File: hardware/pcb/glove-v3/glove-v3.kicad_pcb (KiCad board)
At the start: 2 copper layers, 18 parts, among them U1 XIAO-ESP32C3, U2 CD74HC4067M96

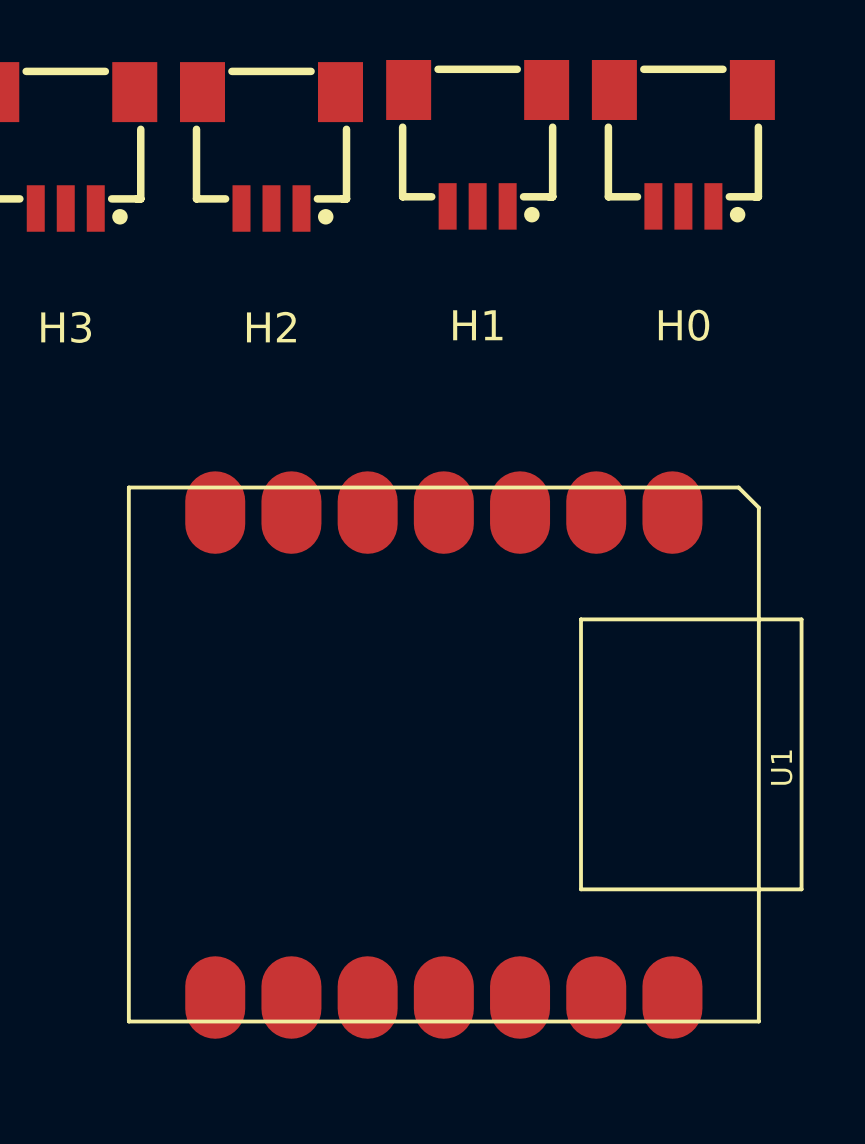
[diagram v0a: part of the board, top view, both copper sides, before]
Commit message: added decoupling capacitor and updated footprints
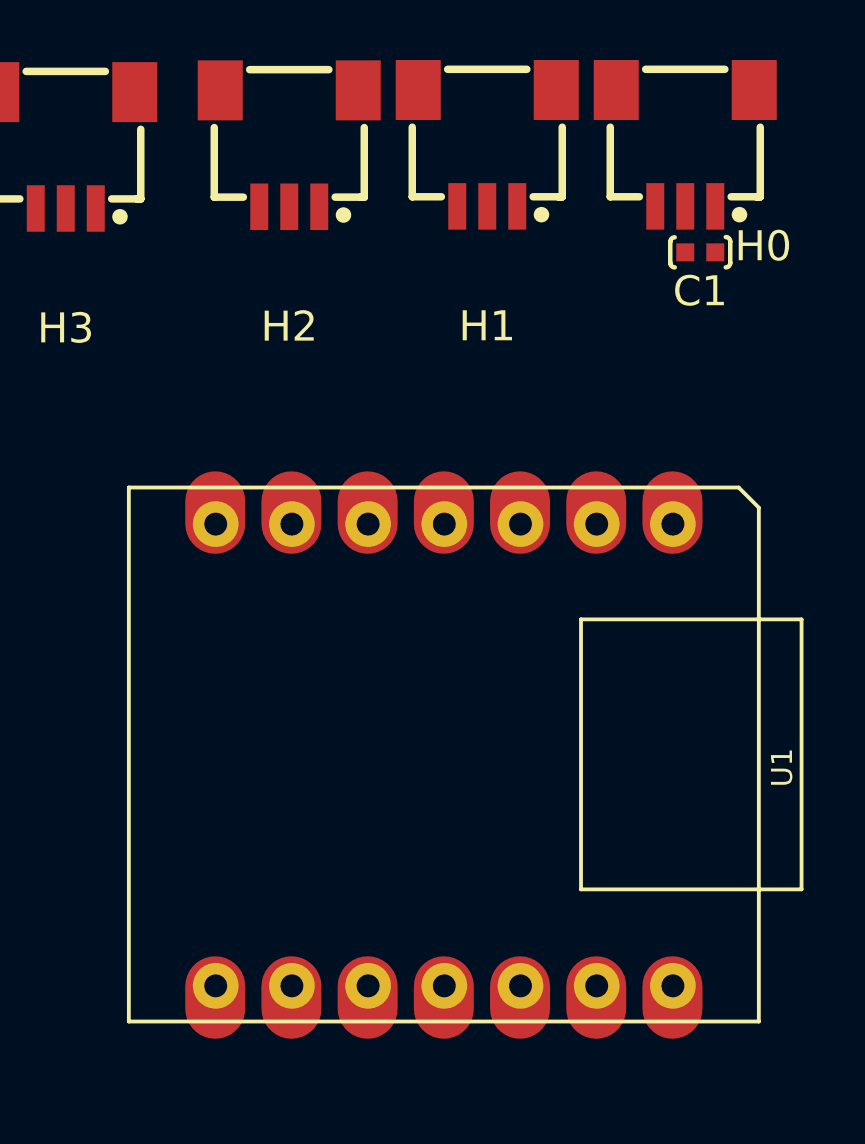
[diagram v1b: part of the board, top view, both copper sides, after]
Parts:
- added C1: C-0402-0.01uF, 0_easyeda2kicad:C0402, F.Cu at (177.6, 37.6)
- moved H2 0.59 mm to (163.9, 34.1)
- moved H1 0.32 mm to (170.5, 34.1)
- moved H0 0.06 mm to (177.1, 34.1)

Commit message: schematic done and board layout done
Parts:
- added C0: C-0402-0.01uF, 0_easyeda2kicad:C0402, F.Cu at (108.6, 56.2)
- added C10: C-0402-0.01uF, 0_easyeda2kicad:C0402, F.Cu at (143.7, 31.9)
- added C11: C-0402-0.01uF, 0_easyeda2kicad:C0402, F.Cu at (150.2, 31.9)
- added C12: C-0402-0.01uF, 0_easyeda2kicad:C0402, F.Cu at (156.7, 31.9)
- added C13: C-0402-0.01uF, 0_easyeda2kicad:C0402, F.Cu at (163.2, 31.9)
- added C14: C-0402-0.01uF, 0_easyeda2kicad:C0402, F.Cu at (169.7, 31.9)
- added C15: C-0402-0.01uF, 0_easyeda2kicad:C0402, F.Cu at (176.2, 31.9)
- added C2: C-0402-0.01uF, 0_easyeda2kicad:C0402, F.Cu at (108.6, 43.2)
- added C3: C-0402-0.01uF, 0_easyeda2kicad:C0402, F.Cu at (108.6, 36.7)
- added C4: C-0402-0.01uF, 0_easyeda2kicad:C0402, F.Cu at (104.7, 31.9)
- added C5: C-0402-0.01uF, 0_easyeda2kicad:C0402, F.Cu at (111.2, 31.9)
- added C6: C-0402-0.01uF, 0_easyeda2kicad:C0402, F.Cu at (117.7, 31.9)
- added C7: C-0402-0.01uF, 0_easyeda2kicad:C0402, F.Cu at (124.2, 31.9)
- added C8: C-0402-0.01uF, 0_easyeda2kicad:C0402, F.Cu at (130.7, 31.9)
- added C9: C-0402-0.01uF, 0_easyeda2kicad:C0402, F.Cu at (137.2, 31.9)
- added REF**: MountingHole_2.2mm_M2_DIN965_Pad, 0_MountingHole:MountingHole_2.2mm_M2_DIN965_Pad, F.Cu at (114.0, 34.5)
- added REF**: MountingHole_2.2mm_M2_DIN965_Pad, 0_MountingHole:MountingHole_2.2mm_M2_DIN965_Pad, F.Cu at (178.1, 57.0)
- added REF**: MountingHole_2.2mm_M2_DIN965_Pad, 0_MountingHole:MountingHole_2.2mm_M2_DIN965_Pad, F.Cu at (114.0, 57.0)
- added REF**: MountingHole_2.2mm_M2_DIN965_Pad, 0_MountingHole:MountingHole_2.2mm_M2_DIN965_Pad, F.Cu at (178.1, 34.5)
- moved H15 84.0 mm to (176.7, 28.4), turned to 180 degrees
- moved H14 75.3 mm to (170.2, 28.4), turned to 180 degrees
- moved H0 75.2 mm to (105.1, 55.7), turned to -90 degrees
- moved C1 70.1 mm to (108.6, 49.7), turned to -90 degrees
- moved H1 67.1 mm to (105.1, 49.2), turned to -90 degrees
- moved H13 66.9 mm to (163.7, 28.4), turned to 180 degrees
- moved H2 59.4 mm to (105.1, 42.7), turned to -90 degrees
- moved H12 58.8 mm to (157.2, 28.4), turned to 180 degrees
- moved H11 51.5 mm to (150.7, 28.4)
- moved H3 51.4 mm to (105.1, 36.2), turned to -90 degrees
- moved H4 44.5 mm to (105.2, 28.4)
- moved H10 38.0 mm to (144.2, 28.4)
- moved H5 31.1 mm to (111.7, 28.4)
- moved H9 24.6 mm to (137.7, 28.4)
- moved H6 17.9 mm to (118.2, 28.4)
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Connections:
- H0 pad 1: +3V3 -> /HALL_0
- H0 pad 3: /HALL_0 -> +3V3
- H1 pad 1: +3V3 -> /HALL_1
- H1 pad 3: /HALL_0 -> +3V3
- H10 pad 1: +3V3 -> /HALL_10
- H10 pad 3: /HALL_0 -> +3V3
- H11 pad 1: +3V3 -> /HALL_11
- H11 pad 3: /HALL_0 -> +3V3
- H12 pad 1: +3V3 -> /HALL_12
- H12 pad 3: /HALL_0 -> +3V3
- H13 pad 1: +3V3 -> /HALL_13
- H13 pad 3: /HALL_0 -> +3V3
- H14 pad 1: +3V3 -> /HALL_14
- H14 pad 3: /HALL_0 -> +3V3
- H15 pad 1: +3V3 -> /HALL_15
- H15 pad 3: /HALL_0 -> +3V3
- H2 pad 1: +3V3 -> /HALL_2
- H2 pad 3: /HALL_0 -> +3V3
- H3 pad 1: +3V3 -> /HALL_3
- H3 pad 3: /HALL_0 -> +3V3
- H4 pad 1: +3V3 -> /HALL_4
- H4 pad 3: /HALL_0 -> +3V3
- H5 pad 1: +3V3 -> /HALL_5
- H5 pad 3: /HALL_0 -> +3V3
- H6 pad 1: +3V3 -> /HALL_6
- H6 pad 3: /HALL_0 -> +3V3
- H7 pad 1: +3V3 -> /HALL_7
- H7 pad 3: /HALL_0 -> +3V3
- H8 pad 1: +3V3 -> /HALL_8
- H8 pad 3: /HALL_0 -> +3V3
- H9 pad 1: +3V3 -> /HALL_9
- H9 pad 3: /HALL_0 -> +3V3
- U1 pad 10: unconnected-(U1-PA5_A9_D9_MISO-Pad10) -> /S0
- U1 pad 12: unconnected-(U1-3V3-Pad12) -> +3V3
- U1 pad 13: unconnected-(U1-GND-Pad13) -> GND
- U1 pad 3: unconnected-(U1-PA10_A2_D2-Pad3) -> /MUX_OUT
- U1 pad 5: unconnected-(U1-PA8_A4_D4_SDA-Pad5) -> /S2
- U1 pad 6: unconnected-(U1-PA9_A5_D5_SCL-Pad6) -> /S3
- U1 pad 9: unconnected-(U1-PA7_A8_D8_SCK-Pad9) -> /S1
- U2 pad 1: unconnected-(U2-COMMONINPUT/OUTPUT-Pad1) -> /MUX_OUT
- U2 pad 10: unconnected-(U2-S0-Pad10) -> /S0
- U2 pad 11: unconnected-(U2-S1-Pad11) -> /S1
- U2 pad 12: unconnected-(U2-GND-Pad12) -> GND
- U2 pad 13: unconnected-(U2-S3-Pad13) -> /S3
- U2 pad 14: unconnected-(U2-S2-Pad14) -> /S2
- U2 pad 15: unconnected-(U2-~{E}-Pad15) -> GND
- U2 pad 16: unconnected-(U2-I15-Pad16) -> /HALL_15
- U2 pad 17: unconnected-(U2-I14-Pad17) -> /HALL_14
- U2 pad 18: unconnected-(U2-I13-Pad18) -> /HALL_13
- U2 pad 19: unconnected-(U2-I12-Pad19) -> /HALL_12
- U2 pad 2: unconnected-(U2-I7-Pad2) -> /HALL_7
- U2 pad 20: unconnected-(U2-I11-Pad20) -> /HALL_11
- U2 pad 21: unconnected-(U2-I10-Pad21) -> /HALL_10
- U2 pad 22: unconnected-(U2-I9-Pad22) -> /HALL_9
- U2 pad 23: unconnected-(U2-I8-Pad23) -> /HALL_8
- U2 pad 24: unconnected-(U2-VCC-Pad24) -> +3V3
- U2 pad 3: unconnected-(U2-I6-Pad3) -> /HALL_6
- U2 pad 4: unconnected-(U2-I5-Pad4) -> /HALL_5
- U2 pad 5: unconnected-(U2-I4-Pad5) -> /HALL_4
- U2 pad 6: unconnected-(U2-I3-Pad6) -> /HALL_3
- U2 pad 7: unconnected-(U2-I2-Pad7) -> /HALL_2
- U2 pad 8: unconnected-(U2-I1-Pad8) -> /HALL_1
- U2 pad 9: unconnected-(U2-I0-Pad9) -> /HALL_0
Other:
- board outline added: 79 x 34.8 mm
- copper layers 2 -> 4

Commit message: glove-v3.0 done and ordered on JLCPCB
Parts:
- added C16: C-0402-0.1uF, 0_easyeda2kicad:C0402, F.Cu at (139.2, 38.5)
- added G***: LOGO, 0_logos:hf-logo, F.Cu at (133.7, 45.5)
- added G***: LOGO, 0_logos:prototype-glove, B.Cu at (126.8, 45.5)
- added G***: LOGO, 0_logos:hand, B.Cu at (126.9, 45.5)
- added U3: 2.5x3mm-BUTTON, 0_easyeda2kicad:KEY-SMD_L3.0-W2.5-LS4.0_TD-1183SN, F.Cu at (151.2, 53.5)
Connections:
- U1 pad 10: /S0 -> /S1
- U1 pad 11: unconnected-(U1-PA6_A10_D10_MOSI-Pad11) -> /S0
- U1 pad 9: /S1 -> Net-(U1-PA7_A8_D8_SCK)
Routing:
- net /HALL_4: track 0.00 -> 51.1 mm
- net /HALL_3: track 0.00 -> 49.8 mm
- net /HALL_2: track 0.00 -> 48.8 mm
- net /HALL_1: track 0.00 -> 47.8 mm
- net /HALL_0: track 0.00 -> 47.4 mm
- net /HALL_5: track 0.00 -> 47.0 mm
- net /HALL_6: track 0.00 -> 41.5 mm
- net /HALL_7: track 0.00 -> 36.7 mm
- net /MUX_OUT: track 0.00 -> 35.1 mm
- net /HALL_15: track 0.00 -> 33.2 mm
- net /HALL_14: track 0.00 -> 26.5 mm
- net +3V3: track 0.00 -> 25.6 mm, vias 0 -> 17
- net /S0: track 0.00 -> 24.9 mm
- net GND: track 0.00 -> 24.5 mm, vias 0 -> 19
- net /HALL_13: track 0.00 -> 21.3 mm
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- added copper zone on In1.Cu, net +3V3
- added copper zone on F.Cu, net GND
- added copper zone on In2.Cu, net GND
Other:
- board size 79 x 34.8 mm -> 79 x 35 mm
- board text added: "@nepyope"
- board text added: "github.com/max-titov"
- board text added: "glove-v3.0"
